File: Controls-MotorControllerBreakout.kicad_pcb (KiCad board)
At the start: 2 copper layers, 47.8 x 44.5 mm, 42 parts, among them J1 MC CAN 1, J2 MC CAN 2, J3 CTRLS, J4 EXT PWR, J5 CANDAPTER, Q1 PMV35EPER, U1 TPS2121RUXR

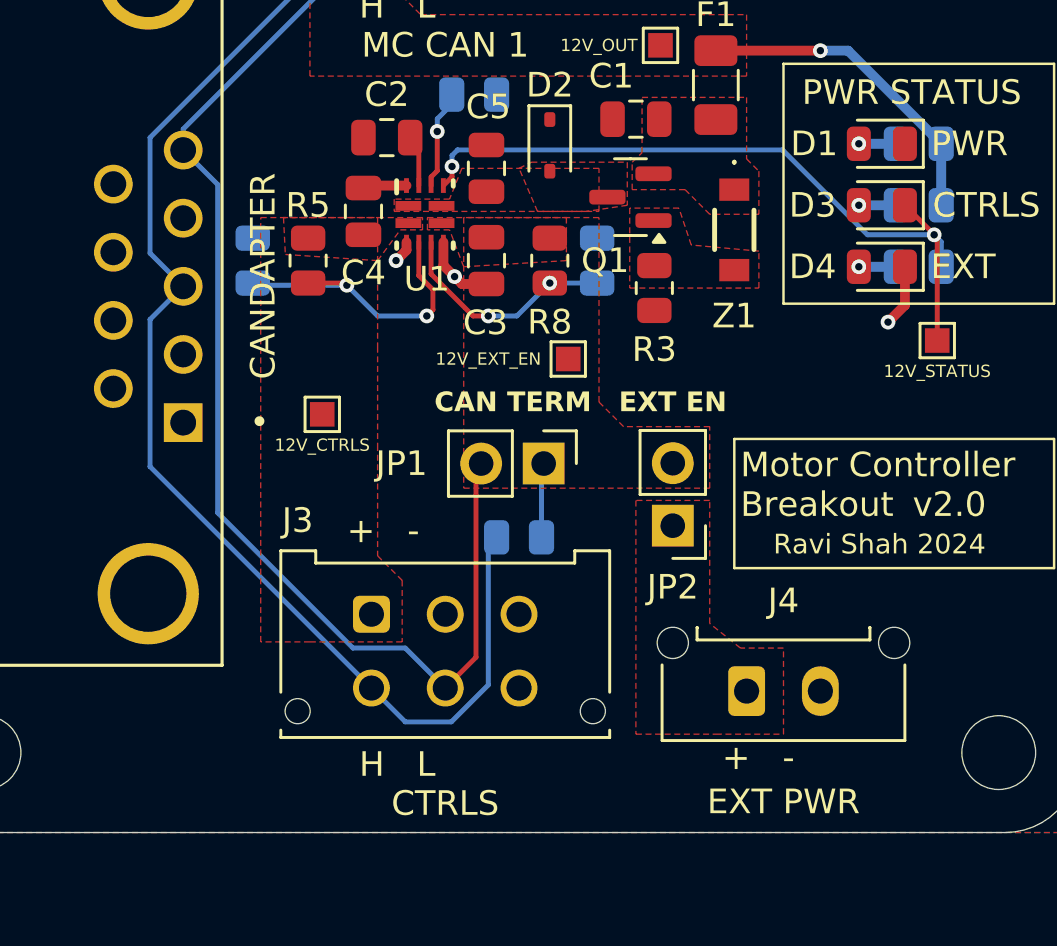
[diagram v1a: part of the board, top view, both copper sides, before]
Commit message: flip connectors so clip faces inside
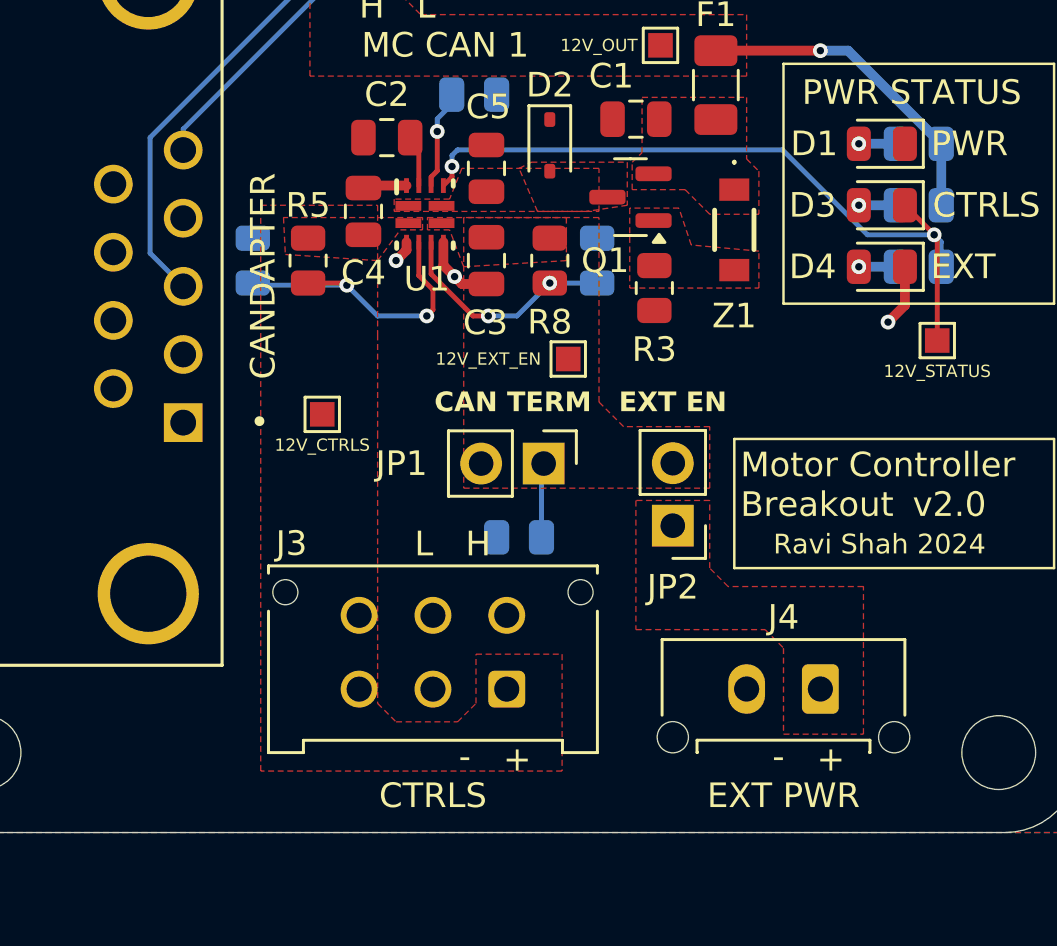
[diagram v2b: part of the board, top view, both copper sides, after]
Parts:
- moved J3 6.29 mm to (97.0, 82.7), turned to 180 degrees
- moved J4 3.00 mm to (109.8, 82.7), turned to 180 degrees
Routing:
- net /CAN_L: track 68.6 -> 31.7 mm
- net /CAN_H: track 68.3 -> 35.6 mm
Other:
- board text added: "L H"
- board text added: "connectors are all facing the same direction. Might wanna orient them so the connector clips face inward. Consider flipping R5, R8, C3 180 degrees so the pads dont interfere with the zones. add stitching vias for your front and back GND layers (especially in areas around D2 and C1 smaller thing but I would try move test points to edge of board so its easier to access"

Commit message: fml aghsjkasjksdhksjjfd
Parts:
- added C6: 10u, Capacitor_SMD:C_0805_2012Metric, F.Cu at (130.6, 61.6)
- added D5: SD12_SOD323, Diode_SMD:D_SOD-323, F.Cu at (130.6, 64.6)
- added F2: 375mA, Fuse:Fuse_1206_3216Metric, F.Cu at (125.6, 61.7)
- added Q2: PMV35EPER, Package_TO_SOT_SMD:SOT-23, F.Cu at (132.5, 57.8)
- added Q3: RUM001L02T2CL, RUM001L02T2CL:TRANS_RUM001_ROM, F.Cu at (138.1, 73.0)
- added Q4: RE1C001ZPTL, RE1C001ZPTL:TRANS_RE1C001_ROM, F.Cu at (133.9, 73.4)
- added R11: 100k, Resistor_SMD:R_0805_2012Metric, F.Cu at (125.0, 64.8)
- added R12: 5k, Resistor_SMD:R_0805_2012Metric, F.Cu at (128.1, 69.8)
- added R13: 51k, Resistor_SMD:R_0805_2012Metric, F.Cu at (128.1, 72.7)
- added R15: 15k, Resistor_SMD:R_0805_2012Metric, F.Cu at (134.5, 69.8)
- added TP3: GND, TestPoint:TestPoint_Pad_1.0x1.0mm, F.Cu at (124.3, 69.8)
- added TP6: GND, TestPoint:TestPoint_Pad_1.0x1.0mm, F.Cu at (124.3, 72.9)
- added Z2: BZT52-B12-QX, Zener:BZT52B12QX, F.Cu at (126.4, 57.7)
- TP1: value 12V_EXT_EN -> EXT
- TP2: value 12V_CTRLS -> CTRLS
- TP5: value 12V_STATUS -> STATUS
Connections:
- C3 pad 1: /PowerDist/+12V_EXT_EN -> /PowerDist/+12V_EXT_PROT
- C4 pad 1: /+12V_CTRLS -> /PowerDist/+12V_CTRLS_PROT
- C5 pad 1: /PowerDist/+12V_SEL -> +12V
- D2 pad 2: /PowerDist/+12V_SEL -> /+12V_CTRLS
- D3 pad 1: /+12V_STATUS -> Net-(D3-K)
- F1 pad 2: +12V -> /PowerDist/+12V_CTRLS_PROT
- Q1 pad 3: /PowerDist/+12V_SEL -> /+12V_CTRLS
- R10 pad 1: /+12V_STATUS -> Net-(Q4-S)
- R5 pad 1: /+12V_CTRLS -> /PowerDist/+12V_EXT_PROT
- R8 pad 1: /PowerDist/+12V_EXT_EN -> /PowerDist/+12V_CTRLS_PROT
- TP1 pad 1: /PowerDist/+12V_EXT_EN -> /PowerDist/+12V_EXT_PROT
- TP2 pad 1: /+12V_CTRLS -> /PowerDist/+12V_CTRLS_PROT
- U1 pad 1: /PowerDist/+12V_SEL -> +12V
- U1 pad 2: /+12V_CTRLS -> /PowerDist/+12V_EXT_PROT
- U1 pad 6: GND -> /PowerDist/PR1
- U1 pad 7: /PowerDist/+12V_EXT_EN -> /PowerDist/+12V_CTRLS_PROT
- U1 pad 8: /PowerDist/+12V_SEL -> +12V
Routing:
- removed copper zone on F.Cu, net /PowerDist/+12V_SEL

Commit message: start layouting again
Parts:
- removed LOGO2: WS Motor Interface, Wavesculptor_Motor_Interface:Wavesculptor_Motor_Interface_Type_1
- moved Q4 160.4 mm to (20.2, 186.5)
- moved Q3 160.4 mm to (24.4, 186.1)
- moved R15 160.4 mm to (20.8, 182.9)
- moved D1 143.3 mm to (36.6, 182.2)
- moved D3 143.3 mm to (36.6, 184.7)
- moved D4 143.3 mm to (36.6, 187.2)
- moved R10 143.3 mm to (38.1, 187.2)
- moved R2 143.3 mm to (38.1, 182.2)
- moved R9 143.3 mm to (38.1, 184.7)
- moved TP4 135.2 mm to (197.8, 153.2)
- moved TP2 131.1 mm to (192.7, 152.4)
- moved TP1 125.1 mm to (196.4, 148.4)
- moved F2 118.0 mm to (135.4, 179.4)
- moved Z2 118.0 mm to (136.2, 175.4)
- moved C6 118.0 mm to (140.4, 179.2)
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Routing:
- net /CAN_H: track 35.6 -> 0.00 mm
- net /CAN_L: track 31.7 -> 0.00 mm
- net /+12V_STATUS: track 30.0 -> 0.00 mm, vias 2 -> 0
- net +12V: track 13.2 -> 0.00 mm, vias 1 -> 0
- net /PowerDist/OV2: track 12.6 -> 0.00 mm, vias 2 -> 0
- net /PowerDist/OV1: track 9.30 -> 0.00 mm, vias 2 -> 0
- net GND: track 8.26 -> 0.00 mm, vias 3 -> 0
- net /PowerDist/ILM: track 4.05 -> 0.00 mm, vias 1 -> 0
- net Net-(JP1-A): track 3.04 -> 0.00 mm
- net /PowerDist/CSS: track 2.09 -> 0.00 mm
- net Net-(D4-A): track 1.53 -> 0.00 mm, vias 1 -> 0
- net Net-(D3-A): track 1.53 -> 0.00 mm, vias 1 -> 0
- net Net-(D1-A): track 1.53 -> 0.00 mm, vias 1 -> 0
- removed copper zone on F.Cu, net /PowerDist/+12V_EXT_EN
- removed copper zone on F.Cu, net Net-(Q1-G)
- removed copper zone on F.Cu, net Net-(Q1-S)
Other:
- board text added: "Consider flipping R5, R8, C3 180 degrees so the pads dont interfere with the zones. add stitching vias for your front and back GND layers (especially in areas around D2 and C1 smaller thing but I would try move test points to edge of board so its easier to access"
- board text removed: "connectors are all facing the same direction. Might wanna orient them so the connector clips face inward. Consider flipping R5, R8, C3 180 degrees so the pads dont interfere with the zones. add stitching vias for your front and back GND layers (especially in areas around D2 and C1 smaller thing but I would try move test points to edge of board so its easier to access"

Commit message: new tps2121 layout/zones
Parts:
- R12: moved to B.Cu
- moved R7 64.9 mm to (145.8, 70.2), turned to -90 degrees
- moved C5 63.3 mm to (142.8, 65.0)
- moved C3 63.3 mm to (142.8, 68.8)
- moved JP1 62.2 mm to (36.8, 81.0)
- moved R4 59.9 mm to (145.8, 63.8), turned to 180 degrees
- moved R5 58.3 mm to (140.5, 68.8)
- moved R8 58.1 mm to (150.5, 68.7)
- moved U1 58.1 mm to (145.5, 66.8)
- moved C2 57.0 mm to (145.0, 63.0), turned to 90 degrees
- moved R1 56.7 mm to (41.0, 80.8)
- moved R12 55.2 mm to (148.0, 70.2), turned to -90 degrees
- moved R6 53.2 mm to (143.5, 70.2), turned to -90 degrees
- moved C4 53.0 mm to (148.2, 68.7), turned to -90 degrees
- moved R13 50.9 mm to (152.8, 68.7), turned to -90 degrees
- moved F2 11.3 mm to (145.0, 173.4), turned to 90 degrees
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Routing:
- added copper zone on F.Cu, net /PowerDist/+12V_CTRLS_PROT
- added copper zone on F.Cu, net /PowerDist/+12V_EXT_PROT
- added copper zone on F.Cu, net Net-(Q1-G)
- added copper zone on F.Cu, net Net-(Q1-S)
- added copper zone on F.Cu, net Net-(Q2-G)
- added copper zone on F.Cu, net Net-(Q2-S)

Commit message: layout redone
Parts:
- R13, R5, R8: moved to B.Cu
- moved TP4 154.6 mm to (85.8, 46.8)
- moved TP3 147.5 mm to (82.2, 46.8)
- moved Q4 145.5 mm to (94.7, 61.5), turned to -90 degrees
- moved D4 141.3 mm to (101.1, 61.5)
- moved D3 141.0 mm to (101.1, 59.2)
- moved Q3 140.8 mm to (94.3, 63.8), turned to -90 degrees
- moved D1 140.8 mm to (101.1, 57.0)
- moved R15 140.2 mm to (91.8, 62.1), turned to -90 degrees
- moved R10 139.8 mm to (99.2, 61.5), turned to 0 degrees
- moved R9 139.5 mm to (99.2, 59.2), turned to 0 degrees
- moved R2 139.3 mm to (99.2, 57.0), turned to 0 degrees
- moved TP5 126.3 mm to (98.0, 64.0)
- moved TP6 124.8 mm to (82.5, 86.0)
- moved R3 123.4 mm to (112.8, 59.2), turned to -90 degrees
- moved TP1 121.5 mm to (97.5, 77.8)
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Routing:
- net /CAN_L: track 0.00 -> 102.6 mm
- net /CAN_H: track 0.00 -> 96.9 mm
- net /+12V_STATUS: track 0.00 -> 19.0 mm, vias 0 -> 3
- net +12V: track 0.00 -> 12.7 mm, vias 0 -> 1
- net /PowerDist/PR1: track 0.00 -> 11.0 mm, vias 0 -> 1
- net /PowerDist/+12V_EXT_PROT: track 0.00 -> 9.86 mm, vias 0 -> 2
- net /PowerDist/OV1: track 0.00 -> 9.26 mm, vias 0 -> 1
- net Net-(D3-K): track 0.00 -> 9.06 mm
- net /PowerDist/OV2: track 0.00 -> 7.95 mm, vias 0 -> 1
- net GND: track 0.00 -> 7.18 mm, vias 0 -> 27
- net /PowerDist/+12V_CTRLS_PROT: track 0.00 -> 3.00 mm, vias 0 -> 1
- net Net-(JP1-A): track 0.00 -> 2.97 mm
- net Net-(Q4-S): track 0.00 -> 2.76 mm, vias 0 -> 1
- net /PowerDist/ILM: track 0.00 -> 2.23 mm, vias 0 -> 1
- net /PowerDist/CSS: track 0.00 -> 1.70 mm
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- added copper zone on B.Cu, net +12V
- added copper zone on F.Cu, net /+12V_STATUS
- added copper zone on F.Cu, net /PowerDist/+12V_EXT_EN
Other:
- board text added: "Motor Controller Interface"
- board text added: "check all silks"
- board text added: "pls work :)"
- board text removed: "Consider flipping R5, R8, C3 180 degrees so the pads dont interfere with the zones. add stitching vias for your front and back GND layers (especially in areas around D2 and C1 smaller thing but I would try move test points to edge of board so its easier to access"
- board text removed: "Motor Controller Breakout"
- board text removed: "daybreak pls work :)"

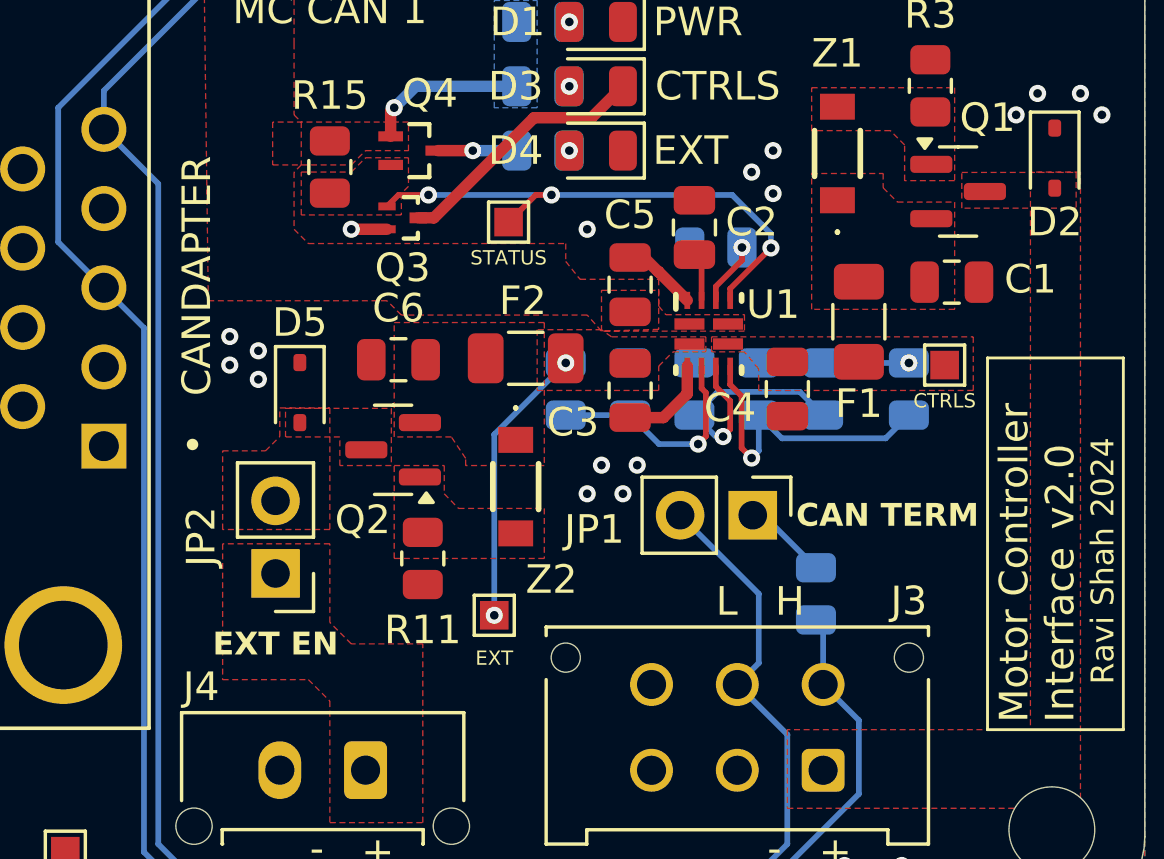
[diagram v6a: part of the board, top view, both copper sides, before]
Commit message: output fuse and solder jumpers
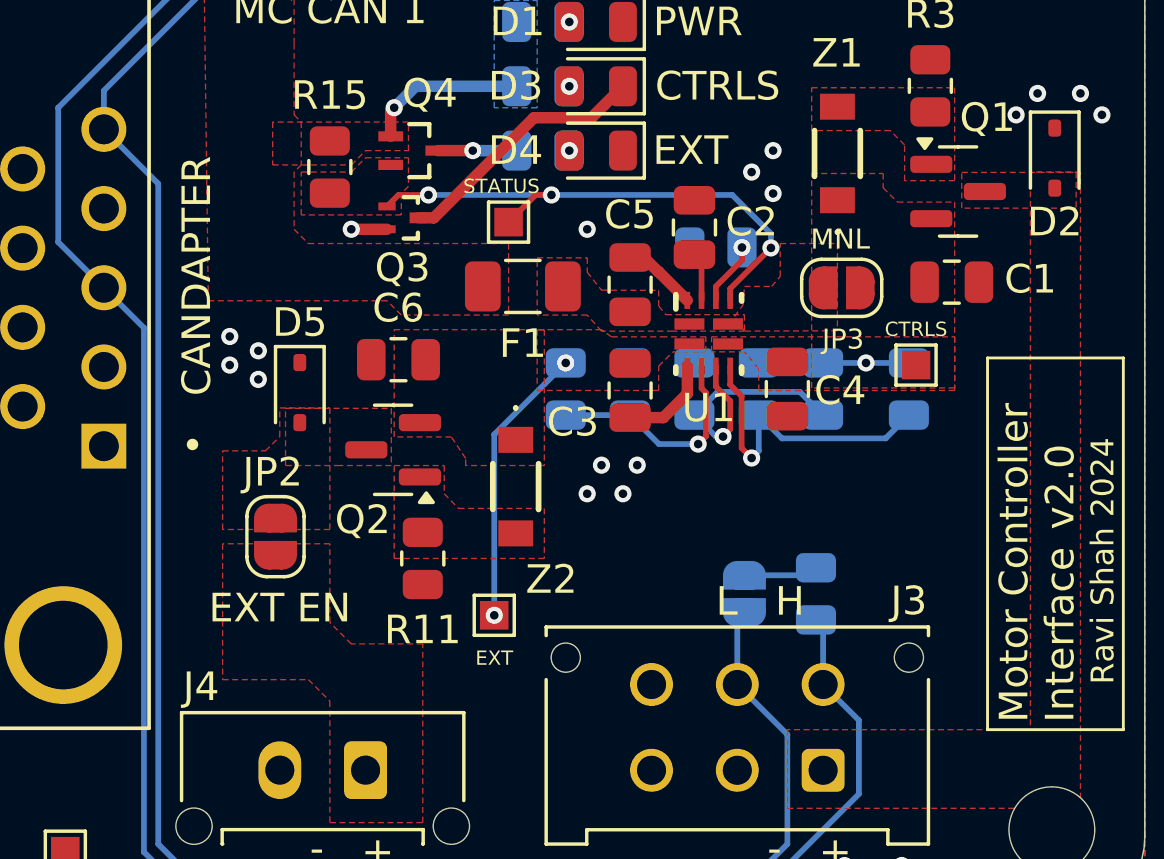
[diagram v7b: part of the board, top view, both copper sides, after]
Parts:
- removed F2: 375mA, Fuse:Fuse_1206_3216Metric
- added JP3: MNL, Jumper:SolderJumper-2_P1.3mm_Open_RoundedPad1.0x1.5mm, F.Cu at (109.7, 66.3)
- JP1: footprint Connector_PinHeader_2.54mm:PinHeader_1x02_P2.54mm_Vertical -> Jumper:SolderJumper-2_P1.3mm_Open_RoundedPad1.0x1.5mm; moved to B.Cu
- JP2: footprint Connector_PinHeader_2.54mm:PinHeader_1x02_P2.54mm_Vertical -> Jumper:SolderJumper-2_P1.3mm_Open_RoundedPad1.0x1.5mm
- moved F1 11.8 mm to (98.5, 66.2), turned to 180 degrees
- moved JP1 2.77 mm to (106.2, 77.0)
- moved JP2 1.29 mm to (89.8, 75.0), turned to 90 degrees
- moved TP2 1.00 mm to (112.2, 69.0)
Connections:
- C1 pad 1: Net-(Q1-S) -> /PowerDist/+12V_CTRLS_PROT
- C5 pad 1: +12V -> /PowerDist/F1-IN
- C6 pad 1: Net-(Q2-S) -> /PowerDist/+12V_EXT_PROT
- F1 pad 1: Net-(Q1-S) -> /PowerDist/F1-IN
- F1 pad 2: /PowerDist/+12V_CTRLS_PROT -> +12V
- Q1 pad 2: Net-(Q1-S) -> /PowerDist/+12V_CTRLS_PROT
- Q2 pad 2: Net-(Q2-S) -> /PowerDist/+12V_EXT_PROT
- U1 pad 1: +12V -> /PowerDist/F1-IN
- U1 pad 8: +12V -> /PowerDist/F1-IN
- Z1 pad 1: Net-(Q1-S) -> /PowerDist/+12V_CTRLS_PROT
- Z2 pad 1: Net-(Q2-S) -> /PowerDist/+12V_EXT_PROT
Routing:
- net /CAN_L: track 102.6 -> 97.9 mm
- added copper zone on F.Cu, net /PowerDist/F1-IN
- removed copper zone on F.Cu, net Net-(Q1-S)
- removed copper zone on F.Cu, net Net-(Q2-S)

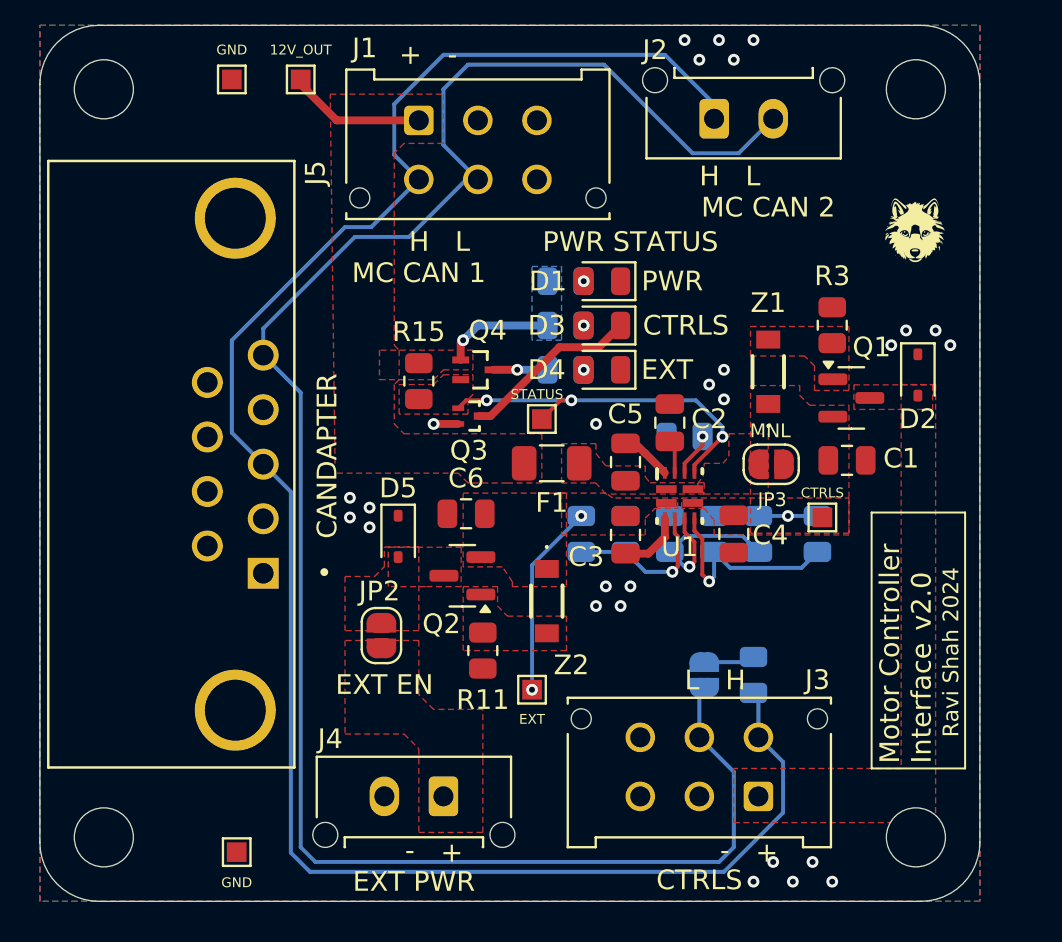
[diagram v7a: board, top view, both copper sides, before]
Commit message: fix silks
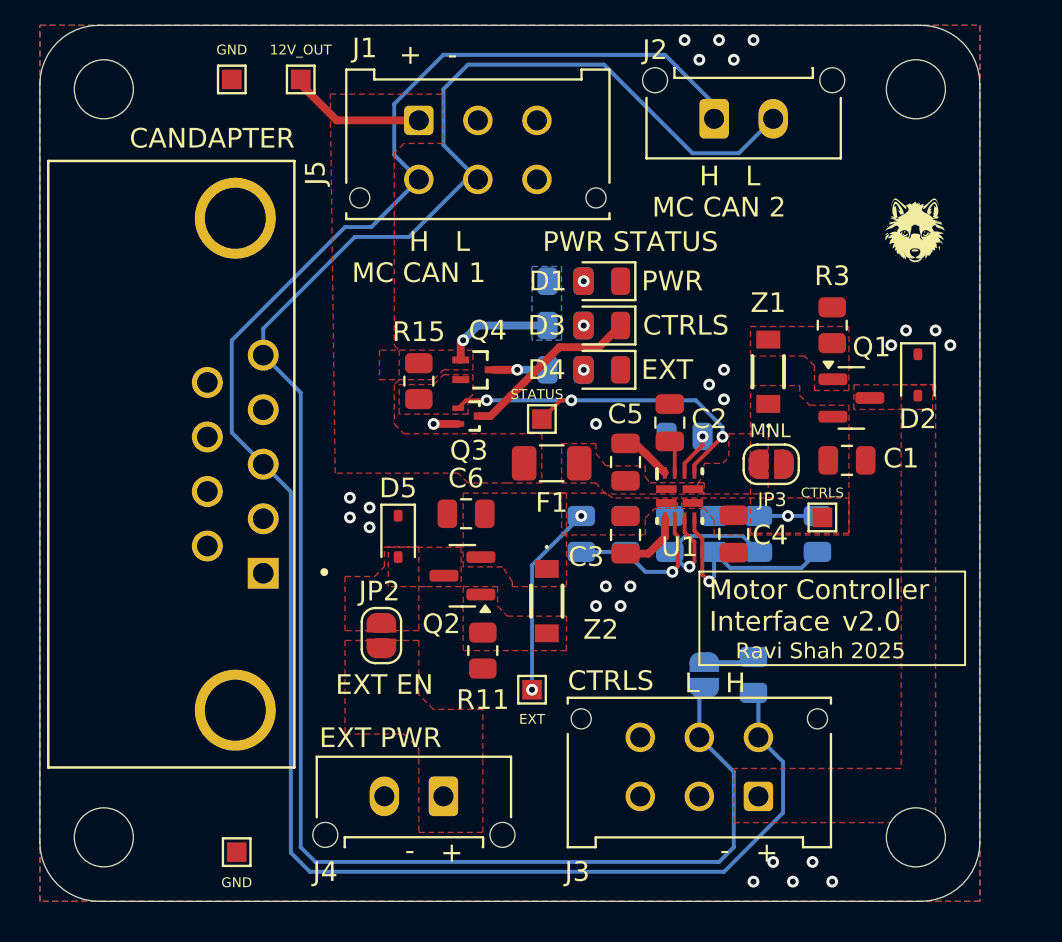
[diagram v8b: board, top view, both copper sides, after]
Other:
- board text added: "Ravi Shah 2025"
- board text removed: "Ravi Shah 2024"
